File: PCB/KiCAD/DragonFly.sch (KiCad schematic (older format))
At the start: 31 parts, among them Q1 MMBFJ310LT1G, Q2 MMBT2222A, T2 1_4, U1 ADE-1, Y1 8Mhz, Y2 8Mhz, Y3 8Mhz, Y4 8Mhz, Y5 8Mhz, Y6 8Mhz

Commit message: diode mixer on discrete components, begin move to DragonFly libs
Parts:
- removed U1: ADE-1, DragonFly:ADE-1H, symbol ADE-1
- added C55: 62, Capacitors_SMD:C_0805, symbol C_Small
- added D8, D9: BAT54S, DragonFly:SOT-23, symbol D_Schottky_x2_Serial_AKC
- added T4, T5: Transformer_1P_2S, DragonFly:HF12, symbol Transformer_1P_2S
- added Y9: 8Mhz, DragonFly:Crystal_HC49-U_Vertical, symbol Crystal_Filter
- C1, C2, C3, C6, C7: footprint Capacitors_SMD:C_0603_HandSoldering -> DragonFly:C_0603_HandSoldering
- D1, D2, D3, D4: footprint Diodes_SMD:D_SOD-323_HandSoldering -> DragonFly:D_SOD-323_HandSoldering
- Q1, Q2: footprint TO_SOT_Packages_SMD:SOT-23 -> DragonFly:SOT-23
- R10, R2: footprint Resistors_SMD:R_0603_HandSoldering -> DragonFly:R_0603_HandSoldering
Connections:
- wire segments 66 -> 93
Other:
- moved on the sheet: C1, C10, C3, C7, C8, D3, D4, L1, Q2, R1, R2, R8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

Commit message: PCB progress, QER filter place, PA place
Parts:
- added C68: 62, Capacitors_SMD:C_0805, symbol C_Small
- added Y10: 8Mhz, DragonFly:Crystal_HC49-U_Vertical, symbol Crystal_Filter
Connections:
- wire segments 93 -> 97
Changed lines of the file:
@@
 $EndComp
 $Comp
-L GND #PWR01
+L GND #PWR3
 U 1 1 58D26266
 P 1100 6250
-F 0 "#PWR01" H 1100 6000 50  0001 C CNN
+F 0 "#PWR3" H 1100 6000 50  0001 C CNN
 F 1 "GND" H 1100 6100 50  0001 C CNN
 F 2 "" H 1100 6250 50  0000 C CNN
@@
 $EndComp
 $Comp
-L GND #PWR02
+L GND #PWR10
 U 1 1 58D27D5F
 P 3850 3400
-F 0 "#PWR02" H 3850 3150 50  0001 C CNN
+F 0 "#PWR10" H 3850 3150 50  0001 C CNN
 F 1 "GND" H 3850 3250 50  0001 C CNN
 F 2 "" H 3850 3400 50  0000 C CNN
@@
 $EndComp
 $Comp
-L GND #PWR03
+L GND #PWR11
 U 1 1 58D27D65
 P 4150 3400
-F 0 "#PWR03" H 4150 3150 50  0001 C CNN
+F 0 "#PWR11" H 4150 3150 50  0001 C CNN
 F 1 "GND" H 4150 3250 50  0001 C CNN
 F 2 "" H 4150 3400 50  0000 C CNN
@@
 $EndComp
 $Comp
-L GND #PWR04
+L GND #PWR17
 U 1 1 58D27D8E
 P 5650 3400
-F 0 "#PWR04" H 5650 3150 50  0001 C CNN
+F 0 "#PWR17" H 5650 3150 50  0001 C CNN
 F 1 "GND" H 5650 3250 50  0001 C CNN
 F 2 "" H 5650 3400 50  0000 C CNN
@@
 $EndComp
 $Comp
-L GND #PWR05
+L GND #PWR9
 U 1 1 58D27DC7
 P 3650 2550
-F 0 "#PWR05" H 3650 2300 50  0001 C CNN
+F 0 "#PWR9" H 3650 2300 50  0001 C CNN
 F 1 "GND" H 3650 2400 50  0001 C CNN
 F 2 "" H 3650 2550 50  0000 C CNN
@@
 $EndComp
 $Comp
-L GND #PWR06
+L GND #PWR7
 U 1 1 58D27DCD
 P 3550 2550
-F 0 "#PWR06" H 3550 2300 50  0001 C CNN
+F 0 "#PWR7" H 3550 2300 50  0001 C CNN
 F 1 "GND" H 3550 2400 50  0001 C CNN
 F 2 "" H 3550 2550 50  0000 C CNN
@@
 $EndComp
 $Comp
-L GND #PWR07
+L GND #PWR8
 U 1 1 58D27DDA
 P 3550 3200
-F 0 "#PWR07" H 3550 2950 50  0001 C CNN
+F 0 "#PWR8" H 3550 2950 50  0001 C CNN
 F 1 "GND" H 3550 3050 50  0001 C CNN
 F 2 "" H 3550 3200 50  0000 C CNN
@@
 $EndComp
 $Comp
-L GND #PWR08
+L GND #PWR21
 U 1 1 58D27E17
 P 5950 3100
-F 0 "#PWR08" H 5950 2850 50  0001 C CNN
+F 0 "#PWR21" H 5950 2850 50  0001 C CNN
 F 1 "GND" H 5950 2950 50  0001 C CNN
 F 2 "" H 5950 3100 50  0000 C CNN
@@
 $EndComp
 $Comp
-L GND #PWR09
+L GND #PWR19
 U 1 1 58D27E1D
 P 5850 3100
-F 0 "#PWR09" H 5850 2850 50  0001 C CNN
+F 0 "#PWR19" H 5850 2850 50  0001 C CNN
 F 1 "GND" H 5850 2950 50  0001 C CNN
 F 2 "" H 5850 3100 50  0000 C CNN
@@
 $EndComp
 $Comp
-L GND #PWR010
+L GND #PWR18
 U 1 1 58D27E23
 P 5850 2550
-F 0 "#PWR010" H 5850 2300 50  0001 C CNN
+F 0 "#PWR18" H 5850 2300 50  0001 C CNN
 F 1 "GND" H 5850 2400 50  0001 C CNN
 F 2 "" H 5850 2550 50  0000 C CNN
@@
 $EndComp
 $Comp
-L GND #PWR011
+L GND #PWR20
 U 1 1 58D27E29
 P 5950 2550
-F 0 "#PWR011" H 5950 2300 50  0001 C CNN
+F 0 "#PWR20" H 5950 2300 50  0001 C CNN
 F 1 "GND" H 5950 2400 50  0001 C CNN
 F 2 "" H 5950 2550 50  0000 C CNN
@@
 $EndComp
 $Comp
-L GND #PWR012
+L GND #PWR5
 U 1 1 58D27E87
 P 3050 3750
-F 0 "#PWR012" H 3050 3500 50  0001 C CNN
+F 0 "#PWR5" H 3050 3500 50  0001 C CNN
 F 1 "GND" H 3050 3600 50  0001 C CNN
 F 2 "" H 3050 3750 50  0000 C CNN
@@
 $EndComp
 $Comp
-L GND #PWR013
+L GND #PWR6
 U 1 1 58D27EA4
 P 3400 3450
-F 0 "#PWR013" H 3400 3200 50  0001 C CNN
+F 0 "#PWR6" H 3400 3200 50  0001 C CNN
 F 1 "GND" H 3400 3300 50  0001 C CNN
 F 2 "" H 3400 3450 50  0000 C CNN
@@
 Connection ~ 6200 3550
 $Comp
-L GND #PWR014
+L GND #PWR22
 U 1 1 58E0F776
 P 5950 3850
-F 0 "#PWR014" H 5950 3600 50  0001 C CNN
+F 0 "#PWR22" H 5950 3600 50  0001 C CNN
 F 1 "GND" H 5950 3700 50  0001 C CNN
 F 2 "" H 5950 3850 50  0000 C CNN
@@
 $EndComp
 $Comp
-L GND #PWR015
+L GND #PWR23
 U 1 1 58E0F80E
 P 6200 3850
-F 0 "#PWR015" H 6200 3600 50  0001 C CNN
+F 0 "#PWR23" H 6200 3600 50  0001 C CNN
 F 1 "GND" H 6200 3700 50  0001 C CNN
 F 2 "" H 6200 3850 50  0000 C CNN
@@
 Connection ~ 2050 3650
 $Comp
-L +12V #PWR016
+L +12V #PWR1
 U 1 1 60FB2C17
 P 900 4200
-F 0 "#PWR016" H 900 4050 50  0001 C CNN
+F 0 "#PWR1" H 900 4050 50  0001 C CNN
 F 1 "+12V" V 900 4450 50  0000 C CNN
 F 2 "" H 900 4200 50  0001 C CNN
@@
 Connection ~ 2500 4000
 $Comp
-L GND #PWR017
+L GND #PWR13
 U 1 1 60FB3F2B
 P 5250 5050
-F 0 "#PWR017" H 5250 4800 50  0001 C CNN
+F 0 "#PWR13" H 5250 4800 50  0001 C CNN
 F 1 "GND" H 5250 4900 50  0001 C CNN
 F 2 "" H 5250 5050 50  0000 C CNN
@@
 $EndComp
 $Comp
-L GND #PWR018
+L GND #PWR2
 U 1 1 60FB5FB6
 P 1000 4600
-F 0 "#PWR018" H 1000 4350 50  0001 C CNN
+F 0 "#PWR2" H 1000 4350 50  0001 C CNN
 F 1 "GND" H 1000 4450 50  0001 C CNN
 F 2 "" H 1000 4600 50  0000 C CNN
@@
 BPF
 $Comp
-L GND #PWR019
+L GND #PWR15
 U 1 1 60FB7D0A
 P 5450 3100
-F 0 "#PWR019" H 5450 2850 50  0001 C CNN
+F 0 "#PWR15" H 5450 2850 50  0001 C CNN
 F 1 "GND" H 5450 2950 50  0001 C CNN
 F 2 "" H 5450 3100 50  0000 C CNN
@@
 $EndComp
 $Comp
-L GND #PWR020
+L GND #PWR16
 U 1 1 60FB7DCF
 P 5550 3100
-F 0 "#PWR020" H 5550 2850 50  0001 C CNN
+F 0 "#PWR16" H 5550 2850 50  0001 C CNN
 F 1 "GND" H 5550 2950 50  0001 C CNN
 F 2 "" H 5550 3100 50  0000 C CNN
@@
 Connection ~ 2600 5050
 $Comp
-L GND #PWR021
+L GND #PWR4
 U 1 1 6122CB46
 P 2100 4900
-F 0 "#PWR021" H 2100 4650 50  0001 C CNN
+F 0 "#PWR4" H 2100 4650 50  0001 C CNN
 F 1 "GND" H 2100 4750 50  0001 C CNN
 F 2 "" H 2100 4900 50  0000 C CNN
@@
 $EndComp
 $Comp
-L GND #PWR022
+L GND #PWR14
 U 1 1 61235BE2
 P 5350 3400
-F 0 "#PWR022" H 5350 3150 50  0001 C CNN
+F 0 "#PWR14" H 5350 3150 50  0001 C CNN
 F 1 "GND" H 5350 3250 50  0001 C CNN
 F 2 "" H 5350 3400 50  0000 C CNN
@@
 	4350 3150 4350 3100
 Wire Wire Line
-	4400 2950 5400 2950
-Wire Wire Line
 	4050 3150 4050 3100
 Connection ~ 4250 3150
@@
 Connection ~ 3550 3150
 Wire Wire Line
-	3550 3150 4350 3150
+	3550 3150 4700 3150
+$Comp
+L Crystal_Filter Y10
+U 1 1 6126846E
+P 4650 2950
+F 0 "Y10" H 4650 3150 50  0000 C CNN
+F 1 "8Mhz" H 4650 3050 50  0000 C CNN
+F 2 "DragonFly:Crystal_HC49-U_Vertical" H 4650 2950 50  0001 C CNN
+F 3 "" H 4650 2950 50  0000 C CNN
+	1    4650 2950
+	1    0    0    -1
+$EndComp
+Wire Wire Line
+	4550 2950 4400 2950
+Wire Wire Line
+	4600 3150 4600 3100
+Connection ~ 4350 3150
+Wire Wire Line
+	4700 3150 4700 3100
+Connection ~ 4600 3150
+$Comp
+L C_Small C68
+U 1 1 6126942C
+P 4450 3300
+F 0 "C68" H 4550 3300 50  0000 L CNN
+F 1 "62" H 4550 3400 50  0000 L CNN
+F 2 "Capacitors_SMD:C_0805" H 4450 3300 50  0001 C CNN
+F 3 "" H 4450 3300 50  0000 C CNN
+	1    4450 3300
+	-1   0    0    1
+$EndComp
+$Comp
+L GND #PWR12
+U 1 1 612694BA
+P 4450 3400
+F 0 "#PWR12" H 4450 3150 50  0001 C CNN
+F 1 "GND" H 4450 3250 50  0001 C CNN
+F 2 "" H 4450 3400 50  0000 C CNN
+F 3 "" H 4450 3400 50  0000 C CNN
+	1    4450 3400
+	1    0    0    -1
+$EndComp
+Wire Wire Line
+	4450 3200 4450 2950
+Connection ~ 4450 2950
+Wire Wire Line
+	4750 2950 5400 2950
 $EndSCHEMATC

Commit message: PCB progress, fix MMBFJ310 error
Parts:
- removed Q1: MMBFJ310LT1G, DragonFly:SOT-23, symbol Q_NJFET_SDG
- added Q1: MMBFJ310LT1G, DragonFly:SOT-23, symbol Q_NJFET_DSG
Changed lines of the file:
@@
 $EndComp
 $Comp
-L GND #PWR01
+L GND #PWR3
 U 1 1 58D26266
 P 1100 6250
-F 0 "#PWR01" H 1100 6000 50  0001 C CNN
+F 0 "#PWR3" H 1100 6000 50  0001 C CNN
 F 1 "GND" H 1100 6100 50  0001 C CNN
 F 2 "" H 1100 6250 50  0000 C CNN
@@
 $EndComp
 $Comp
-L GND #PWR02
+L GND #PWR10
 U 1 1 58D27D5F
 P 3850 3400
-F 0 "#PWR02" H 3850 3150 50  0001 C CNN
+F 0 "#PWR10" H 3850 3150 50  0001 C CNN
 F 1 "GND" H 3850 3250 50  0001 C CNN
 F 2 "" H 3850 3400 50  0000 C CNN
@@
 $EndComp
 $Comp
-L GND #PWR03
+L GND #PWR11
 U 1 1 58D27D65
 P 4150 3400
-F 0 "#PWR03" H 4150 3150 50  0001 C CNN
+F 0 "#PWR11" H 4150 3150 50  0001 C CNN
 F 1 "GND" H 4150 3250 50  0001 C CNN
 F 2 "" H 4150 3400 50  0000 C CNN
@@
 $EndComp
 $Comp
-L GND #PWR04
+L GND #PWR17
 U 1 1 58D27D8E
 P 5650 3400
-F 0 "#PWR04" H 5650 3150 50  0001 C CNN
+F 0 "#PWR17" H 5650 3150 50  0001 C CNN
 F 1 "GND" H 5650 3250 50  0001 C CNN
 F 2 "" H 5650 3400 50  0000 C CNN
@@
 $EndComp
 $Comp
-L GND #PWR05
+L GND #PWR9
 U 1 1 58D27DC7
 P 3650 2550
-F 0 "#PWR05" H 3650 2300 50  0001 C CNN
+F 0 "#PWR9" H 3650 2300 50  0001 C CNN
 F 1 "GND" H 3650 2400 50  0001 C CNN
 F 2 "" H 3650 2550 50  0000 C CNN
@@
 $EndComp
 $Comp
-L GND #PWR06
+L GND #PWR7
 U 1 1 58D27DCD
 P 3550 2550
-F 0 "#PWR06" H 3550 2300 50  0001 C CNN
+F 0 "#PWR7" H 3550 2300 50  0001 C CNN
 F 1 "GND" H 3550 2400 50  0001 C CNN
 F 2 "" H 3550 2550 50  0000 C CNN
@@
 $EndComp
 $Comp
-L GND #PWR07
+L GND #PWR8
 U 1 1 58D27DDA
 P 3550 3200
-F 0 "#PWR07" H 3550 2950 50  0001 C CNN
+F 0 "#PWR8" H 3550 2950 50  0001 C CNN
 F 1 "GND" H 3550 3050 50  0001 C CNN
 F 2 "" H 3550 3200 50  0000 C CNN
@@
 $EndComp
 $Comp
-L GND #PWR08
+L GND #PWR21
 U 1 1 58D27E17
 P 5950 3100
-F 0 "#PWR08" H 5950 2850 50  0001 C CNN
+F 0 "#PWR21" H 5950 2850 50  0001 C CNN
 F 1 "GND" H 5950 2950 50  0001 C CNN
 F 2 "" H 5950 3100 50  0000 C CNN
@@
 $EndComp
 $Comp
-L GND #PWR09
+L GND #PWR19
 U 1 1 58D27E1D
 P 5850 3100
-F 0 "#PWR09" H 5850 2850 50  0001 C CNN
+F 0 "#PWR19" H 5850 2850 50  0001 C CNN
 F 1 "GND" H 5850 2950 50  0001 C CNN
 F 2 "" H 5850 3100 50  0000 C CNN
@@
 $EndComp
 $Comp
-L GND #PWR010
+L GND #PWR18
 U 1 1 58D27E23
 P 5850 2550
-F 0 "#PWR010" H 5850 2300 50  0001 C CNN
+F 0 "#PWR18" H 5850 2300 50  0001 C CNN
 F 1 "GND" H 5850 2400 50  0001 C CNN
 F 2 "" H 5850 2550 50  0000 C CNN
@@
 $EndComp
 $Comp
-L GND #PWR011
+L GND #PWR20
 U 1 1 58D27E29
 P 5950 2550
-F 0 "#PWR011" H 5950 2300 50  0001 C CNN
+F 0 "#PWR20" H 5950 2300 50  0001 C CNN
 F 1 "GND" H 5950 2400 50  0001 C CNN
 F 2 "" H 5950 2550 50  0000 C CNN
@@
 $EndComp
 $Comp
-L GND #PWR012
+L GND #PWR5
 U 1 1 58D27E87
 P 3050 3750
-F 0 "#PWR012" H 3050 3500 50  0001 C CNN
+F 0 "#PWR5" H 3050 3500 50  0001 C CNN
 F 1 "GND" H 3050 3600 50  0001 C CNN
 F 2 "" H 3050 3750 50  0000 C CNN
@@
 $EndComp
 $Comp
-L GND #PWR013
+L GND #PWR6
 U 1 1 58D27EA4
 P 3400 3450
-F 0 "#PWR013" H 3400 3200 50  0001 C CNN
+F 0 "#PWR6" H 3400 3200 50  0001 C CNN
 F 1 "GND" H 3400 3300 50  0001 C CNN
 F 2 "" H 3400 3450 50  0000 C CNN
@@
 	1    6200 3350
 	1    0    0    -1
-$EndComp
-$Comp
-L Q_NJFET_SDG Q1
-U 1 1 58D27EB1
-P 2150 3400
-F 0 "Q1" H 2450 3250 50  0000 L CNN
-F 1 "MMBFJ310LT1G" H 2400 3350 50  0000 L CNN
-F 2 "DragonFly:SOT-23" H -4600 -850 50  0001 C CNN
-F 3 "" H -4800 -950 50  0001 C CNN
-	1    2150 3400
-	-1   0    0    1
 $EndComp
 $Comp
@@
 Connection ~ 6200 3550
 $Comp
-L GND #PWR014
+L GND #PWR22
 U 1 1 58E0F776
 P 5950 3850
-F 0 "#PWR014" H 5950 3600 50  0001 C CNN
+F 0 "#PWR22" H 5950 3600 50  0001 C CNN
 F 1 "GND" H 5950 3700 50  0001 C CNN
 F 2 "" H 5950 3850 50  0000 C CNN
@@
 $EndComp
 $Comp
-L GND #PWR015
+L GND #PWR23
 U 1 1 58E0F80E
 P 6200 3850
-F 0 "#PWR015" H 6200 3600 50  0001 C CNN
+F 0 "#PWR23" H 6200 3600 50  0001 C CNN
 F 1 "GND" H 6200 3700 50  0001 C CNN
 F 2 "" H 6200 3850 50  0000 C CNN
@@
 Connection ~ 2050 3650
 $Comp
-L +12V #PWR016
+L +12V #PWR1
 U 1 1 60FB2C17
 P 900 4200
-F 0 "#PWR016" H 900 4050 50  0001 C CNN
+F 0 "#PWR1" H 900 4050 50  0001 C CNN
 F 1 "+12V" V 900 4450 50  0000 C CNN
 F 2 "" H 900 4200 50  0001 C CNN
@@
 Connection ~ 2500 4000
 $Comp
-L GND #PWR017
+L GND #PWR13
 U 1 1 60FB3F2B
 P 5250 5050
-F 0 "#PWR017" H 5250 4800 50  0001 C CNN
+F 0 "#PWR13" H 5250 4800 50  0001 C CNN
 F 1 "GND" H 5250 4900 50  0001 C CNN
 F 2 "" H 5250 5050 50  0000 C CNN
@@
 $EndComp
 $Comp
-L GND #PWR018
+L GND #PWR2
 U 1 1 60FB5FB6
 P 1000 4600
-F 0 "#PWR018" H 1000 4350 50  0001 C CNN
+F 0 "#PWR2" H 1000 4350 50  0001 C CNN
 F 1 "GND" H 1000 4450 50  0001 C CNN
 F 2 "" H 1000 4600 50  0000 C CNN
@@
 BPF
 $Comp
-L GND #PWR019
+L GND #PWR15
 U 1 1 60FB7D0A
 P 5450 3100
-F 0 "#PWR019" H 5450 2850 50  0001 C CNN
+F 0 "#PWR15" H 5450 2850 50  0001 C CNN
 F 1 "GND" H 5450 2950 50  0001 C CNN
 F 2 "" H 5450 3100 50  0000 C CNN
@@
 $EndComp
 $Comp
-L GND #PWR020
+L GND #PWR16
 U 1 1 60FB7DCF
 P 5550 3100
-F 0 "#PWR020" H 5550 2850 50  0001 C CNN
+F 0 "#PWR16" H 5550 2850 50  0001 C CNN
 F 1 "GND" H 5550 2950 50  0001 C CNN
 F 2 "" H 5550 3100 50  0000 C CNN
@@
 Connection ~ 2600 5050
 $Comp
-L GND #PWR021
+L GND #PWR4
 U 1 1 6122CB46
 P 2100 4900
-F 0 "#PWR021" H 2100 4650 50  0001 C CNN
+F 0 "#PWR4" H 2100 4650 50  0001 C CNN
 F 1 "GND" H 2100 4750 50  0001 C CNN
 F 2 "" H 2100 4900 50  0000 C CNN
@@
 $EndComp
 $Comp
-L GND #PWR022
+L GND #PWR14
 U 1 1 61235BE2
 P 5350 3400
-F 0 "#PWR022" H 5350 3150 50  0001 C CNN
+F 0 "#PWR14" H 5350 3150 50  0001 C CNN
 F 1 "GND" H 5350 3250 50  0001 C CNN
 F 2 "" H 5350 3400 50  0000 C CNN
@@
 $EndComp
 $Comp
-L GND #PWR023
+L GND #PWR12
 U 1 1 612694BA
 P 4450 3400
-F 0 "#PWR023" H 4450 3150 50  0001 C CNN
+F 0 "#PWR12" H 4450 3150 50  0001 C CNN
 F 1 "GND" H 4450 3250 50  0001 C CNN
 F 2 "" H 4450 3400 50  0000 C CNN
@@
 Wire Wire Line
 	4750 2950 5400 2950
+$Comp
+L Q_NJFET_DSG Q1
+U 1 1 612AA96A
+P 2150 3400
+F 0 "Q1" H 2600 3250 50  0000 L CNN
+F 1 "MMBFJ310LT1G" H 2350 3350 50  0000 L CNN
+F 2 "DragonFly:SOT-23" H 2350 3500 50  0001 C CNN
+F 3 "" H 2150 3400 50  0001 C CNN
+	1    2150 3400
+	-1   0    0    1
+$EndComp
 $EndSCHEMATC

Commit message: UR5FFR Mixer FSA3157
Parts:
- removed C3: 100nF, DragonFly:C_0603_HandSoldering, symbol C_Small
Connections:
- net at C2.2, R3.2: no longer T4.4 (SB), T4.5 (SC)
- net +12V: no longer names the net of T5.1 (AA)
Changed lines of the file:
@@
 $Descr A4 11693 8268
 encoding utf-8
-Sheet 1 6
+Sheet 1 7
 Title ""
 Date ""
@@
 	2050 3600 2050 3700
 Connection ~ 2050 3650
-$Comp
-L +12V #PWR1
-U 1 1 60FB2C17
-P 900 4200
-F 0 "#PWR1" H 900 4050 50  0001 C CNN
-F 1 "+12V" V 900 4450 50  0000 C CNN
-F 2 "" H 900 4200 50  0001 C CNN
-F 3 "" H 900 4200 50  0001 C CNN
-	1    900  4200
-	0    -1   -1   0
-$EndComp
 Wire Wire Line
 	2050 3650 2500 3650
@@
 Wire Wire Line
 	2050 3900 2050 4000
-Wire Wire Line
-	2050 4000 4200 4000
 Wire Wire Line
 	2500 3900 2500 4000
@@
 	1400 5950 1650 5950
 Connection ~ 1550 5950
-$Comp
-L C_Small C3
-U 1 1 60FB5DF3
-P 1000 4400
-F 0 "C3" H 700 4400 50  0000 L CNN
-F 1 "100nF" H 700 4300 50  0000 L CNN
-F 2 "DragonFly:C_0603_HandSoldering" H 1000 4400 50  0001 C CNN
-F 3 "" H 1000 4400 50  0000 C CNN
-	1    1000 4400
-	1    0    0    -1
-$EndComp
-$Comp
-L GND #PWR2
-U 1 1 60FB5FB6
-P 1000 4600
-F 0 "#PWR2" H 1000 4350 50  0001 C CNN
-F 1 "GND" H 1000 4450 50  0001 C CNN
-F 2 "" H 1000 4600 50  0000 C CNN
-F 3 "" H 1000 4600 50  0000 C CNN
-	1    1000 4600
-	1    0    0    -1
-$EndComp
-Wire Wire Line
-	1000 4600 1000 4500
 Wire Wire Line
 	1100 6250 1100 6150
@@
 	4300 4650 4200 4650
 Wire Wire Line
-	4200 4000 4200 4850
-Wire Wire Line
 	4200 4850 4300 4850
 Connection ~ 4200 4650
@@
 	1    0    0    -1
 $EndComp
-Wire Wire Line
-	900  4200 1150 4200
-Wire Wire Line
-	1000 4200 1000 4300
 Wire Wire Line
 	1150 4200 1150 4550
@@
 	-1   0    0    1
 $EndComp
+$Sheet
+S 2850 6050 2400 1300
+U 612BEAB5
+F0 "mixer" 60
+F1 "mixer.sch" 60
+$EndSheet
+Wire Wire Line
+	2050 4000 4200 4000
 $EndSCHEMATC

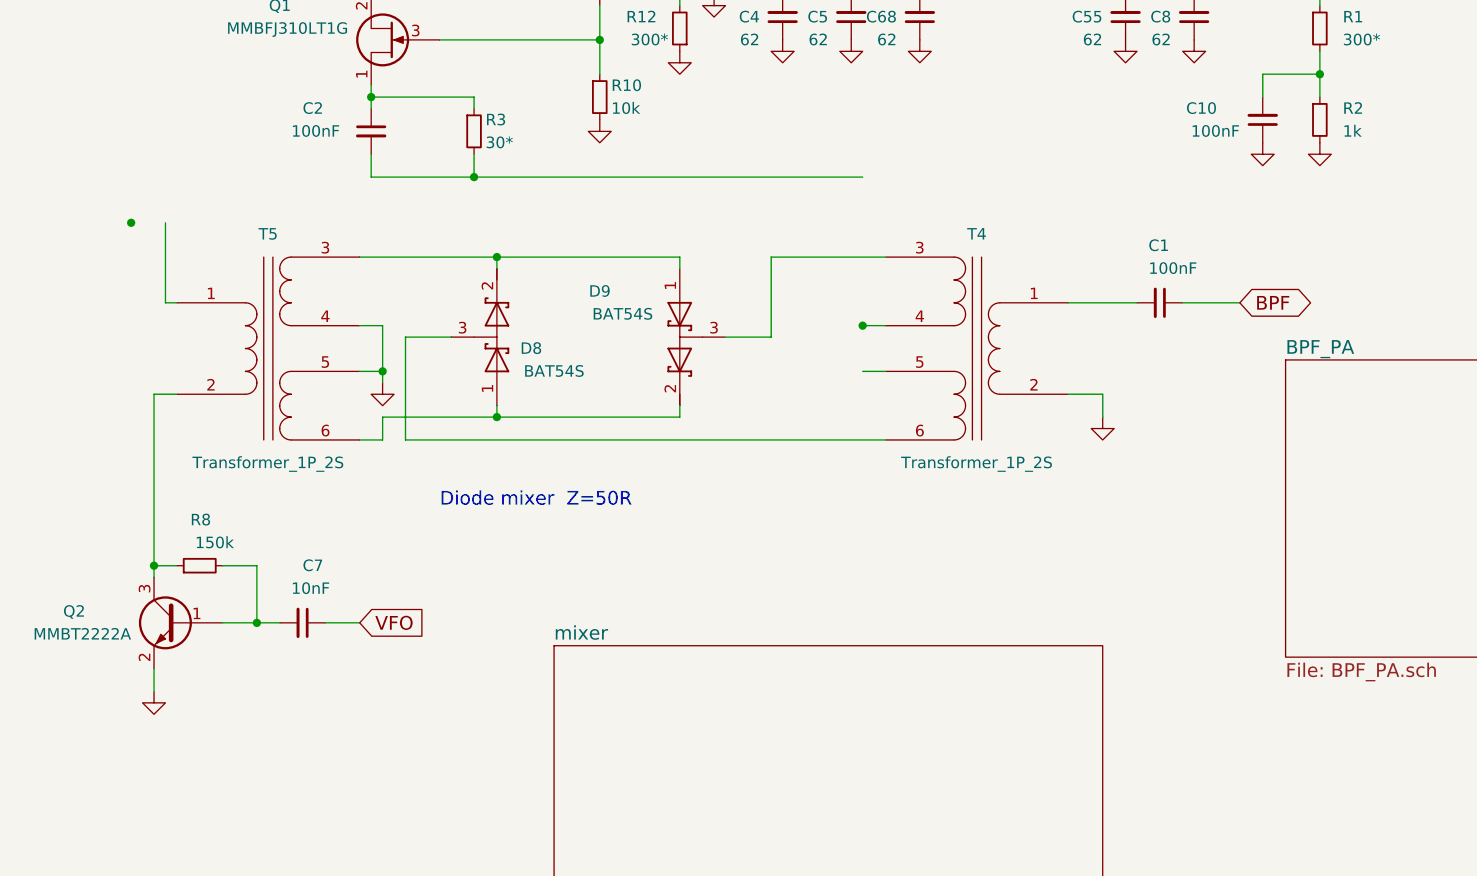
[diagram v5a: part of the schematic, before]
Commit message: mixer schema is done, pcb progress, fix 78l06 issue
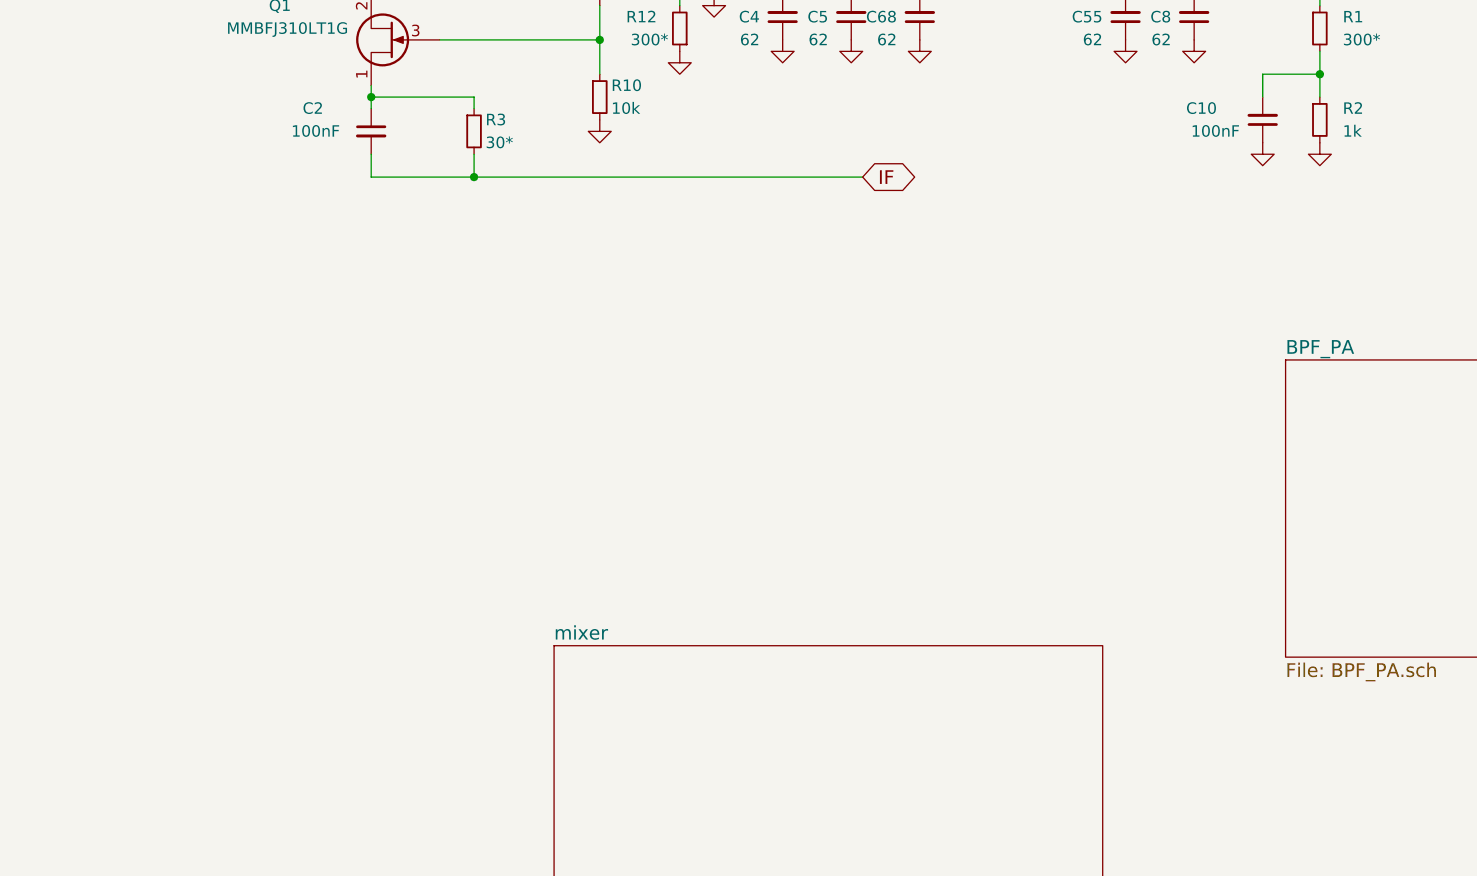
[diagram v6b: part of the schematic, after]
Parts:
- removed C1: 100nF, DragonFly:C_0603_HandSoldering, symbol C_Small
- removed C7: 10nF, DragonFly:C_0603_HandSoldering, symbol C_Small
- removed D8, D9: BAT54S, DragonFly:SOT-23, symbol D_Schottky_x2_Serial_AKC
- removed Q2: MMBT2222A, DragonFly:SOT-23, symbol Q_NPN_BEC
- removed R8: 150k, DragonFly:R_1206_0603, symbol R_Small
- removed T4, T5: Transformer_1P_2S, DragonFly:HF12, symbol Transformer_1P_2S
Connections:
- net IF: now reaches C2.2, R3.2
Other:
- note removed: "Diode mixer Z=50R\n"
